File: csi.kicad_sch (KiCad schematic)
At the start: 65 parts, among them J1 Conn_01x15_MountingPin, J16 Conn_01x15_MountingPin, J6 Conn_01x15_MountingPin, J9 Conn_01x15_MountingPin, U24 AP22615A_TSOT26, U25 AP22615A_TSOT26, U26 PI4MSD5V9548AZDEX, U3 AP22615A_TSOT26, U31 NTS0102_XSON, U32 NTS0102_XSON, U7 AP22615A_TSOT26

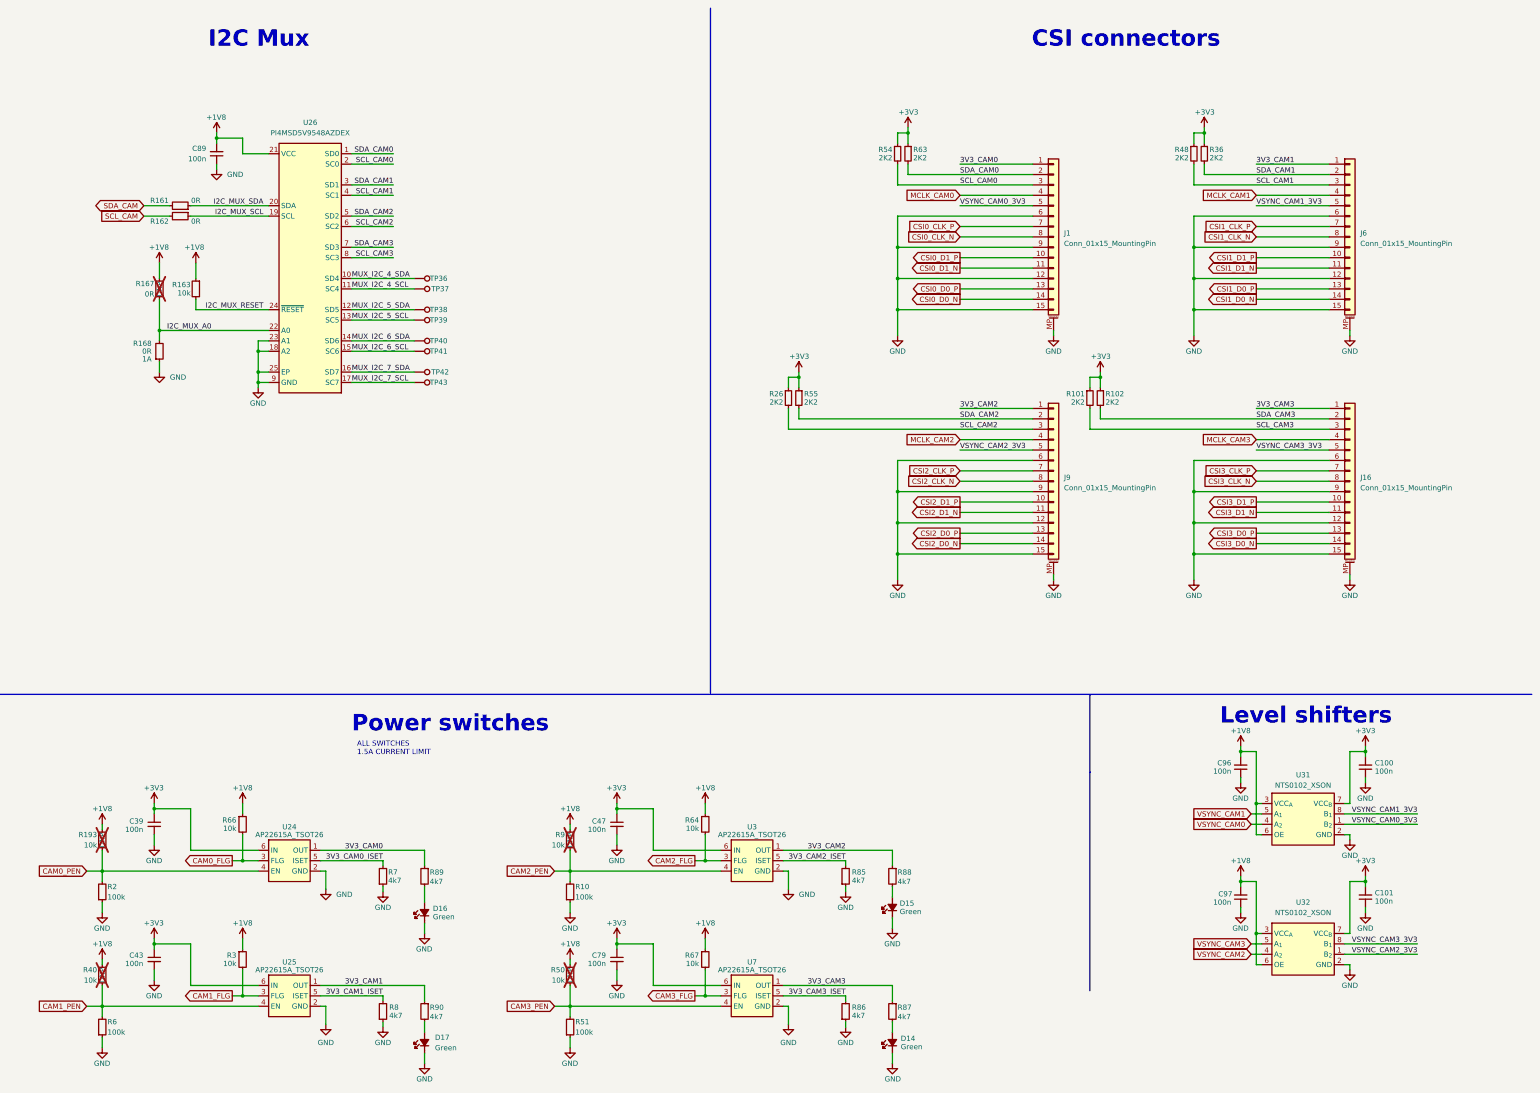
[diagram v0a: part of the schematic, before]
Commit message: Schematic Cleanup, Complete routing
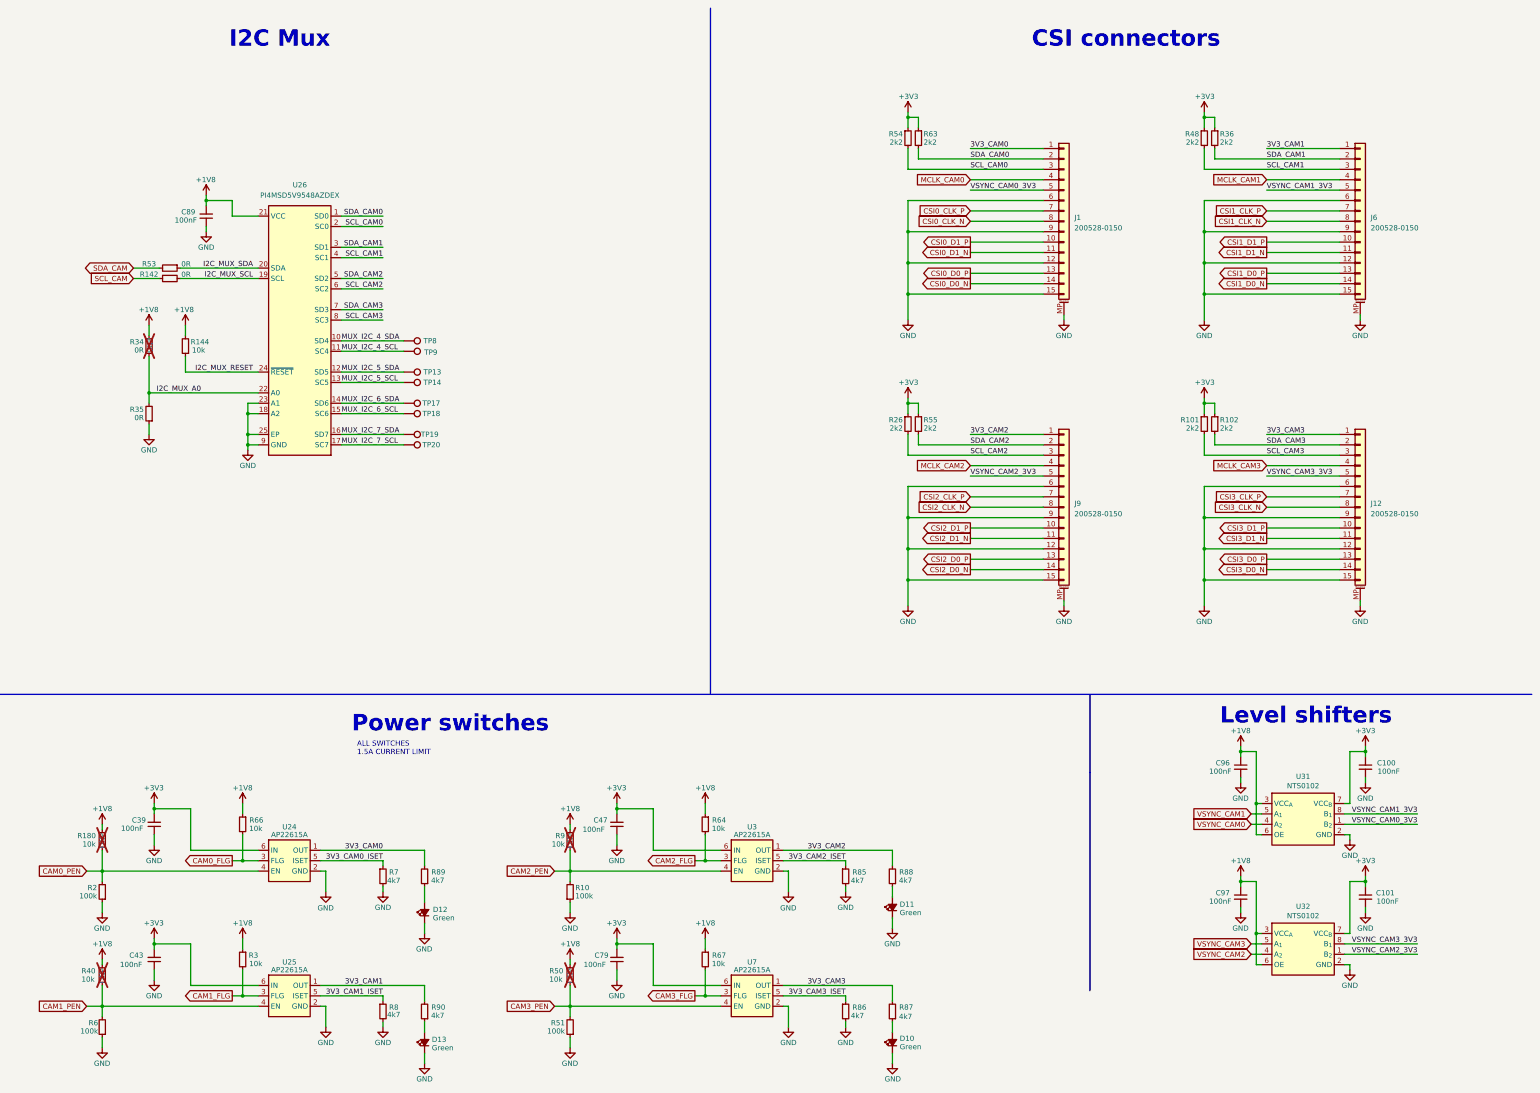
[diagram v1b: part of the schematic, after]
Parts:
- C100, C101, C39, C43, C47, C79, C89, C96, C97: value C_100n_0603 -> 100nF; symbol antmicroCapacitors0402:C_100n_0402 -> Device:C_Small
- D10: renamed from D14; symbol antmicroLEDIndicationDiscrete:LED_G_0603_LTST-C190GKT -> Device:LED_Small_Filled
- D11: renamed from D15; symbol antmicroLEDIndicationDiscrete:LED_G_0603_LTST-C190GKT -> Device:LED_Small_Filled
- D12: renamed from D16; symbol antmicroLEDIndicationDiscrete:LED_G_0603_LTST-C190GKT -> Device:LED_Small_Filled
- D13: renamed from D17; symbol antmicroLEDIndicationDiscrete:LED_G_0603_LTST-C190GKT -> Device:LED_Small_Filled
- J1, J6, J9: value Conn_01x15_MountingPin -> 200528-0150
- J12: renamed from J16; value Conn_01x15_MountingPin -> 200528-0150
- R10, R2, R51, R6: value R_100k_0603 -> 100k; symbol antmicroResistors0402:R_100k_0402 -> Device:R_Small
- R101, R102, R26, R36, R48, R54, R55, R63: value 2K2 -> 2k2
- R142: renamed from R162; value R_0R_0402 -> 0R; symbol antmicroResistors0402:R_0R_0402 -> Device:R_Small
- R144: renamed from R163; value R_10k_0603 -> 10k; symbol antmicroResistors0402:R_10k_0402 -> Device:R_Small
- R180: renamed from R193; value R_10k_0603 -> 10k; symbol antmicroResistors0402:R_10k_0402 -> Device:R_Small; now in the parts list
- R3, R64, R66, R67: value R_10k_0603 -> 10k; symbol antmicroResistors0402:R_10k_0402 -> Device:R_Small
- R34: renamed from R167; value R_0R_0402 -> 0R; symbol antmicroResistors0402:R_0R_0402 -> Device:R_Small; now in the parts list
- R35: renamed from R168; value R_0R_0402 -> 0R; symbol antmicroResistors0402:R_0R_0402 -> Device:R_Small
- R40, R50, R9: value R_10k_0603 -> 10k; symbol antmicroResistors0402:R_10k_0402 -> Device:R_Small; now in the parts list
- R53: renamed from R161; value R_0R_0402 -> 0R; symbol antmicroResistors0402:R_0R_0402 -> Device:R_Small
- R7, R8, R85, R86, R87, R88, R89, R90: value R_4k7_0603 -> 4k7; symbol antmicroResistors0402:R_4k7_0402 -> Device:R_Small
- TP13: renamed from TP38; symbol antmicroTestPoints:TP_0.75mm_SMD -> Connector:TestPoint
- TP14: renamed from TP39; symbol antmicroTestPoints:TP_0.75mm_SMD -> Connector:TestPoint
- TP17: renamed from TP40; symbol antmicroTestPoints:TP_0.75mm_SMD -> Connector:TestPoint
- TP18: renamed from TP41; symbol antmicroTestPoints:TP_0.75mm_SMD -> Connector:TestPoint
- TP19: renamed from TP42; symbol antmicroTestPoints:TP_0.75mm_SMD -> Connector:TestPoint
- TP20: renamed from TP43; symbol antmicroTestPoints:TP_0.75mm_SMD -> Connector:TestPoint
- TP8: renamed from TP36; symbol antmicroTestPoints:TP_0.75mm_SMD -> Connector:TestPoint
- TP9: renamed from TP37; symbol antmicroTestPoints:TP_0.75mm_SMD -> Connector:TestPoint
- U24, U25, U3, U7: value AP22615A_TSOT26 -> AP22615A; symbol antmicroPMICPowerDistributionSwitchesLoadDrivers:AP22615A_TSOT26 -> JetsonCarrier:AP22615A_TSOT26
- U26: symbol antmicroLogicSignalSwitchesMultiplexersDecoders:PI4MSD5V9548AZDEX -> JetsonCarrier:PI4MSD5V9548AZDEX
- U31, U32: value NTS0102_XSON -> NTS0102; symbol antmicroLogicTranslatorsLevelShifters:NTS0102_XSON -> JetsonCarrier:NTS0102
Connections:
- net +1V8: now also C96.1, C97.1, R144.2, R180.1, R40.1, R50.1, R9.1; no longer C96.2, C97.2, R144.1, R180.2, R40.2, R50.2, R9.2
- net +3V3: now also C100.1, C101.1, C39.2, C43.2, C47.2, C79.2; no longer C100.2, C101.2, C39.1, C43.1, C47.1, C79.1
- net 3V3_CAM0: now also R89.2; no longer R89.1
- net 3V3_CAM0_ISET: now also R7.1; no longer R7.2
- net 3V3_CAM1: now also R90.2; no longer R90.1
- net 3V3_CAM1_ISET: now also R8.1; no longer R8.2
- net 3V3_CAM2: now also R88.2; no longer R88.1
- net 3V3_CAM2_ISET: now also R85.1; no longer R85.2
- net 3V3_CAM3: now also R87.2; no longer R87.1
- net 3V3_CAM3_ISET: now also R86.1; no longer R86.2
- net CAM0_PEN: now also R180.2; no longer R180.1
- net CAM1_PEN: now also R40.2; no longer R40.1
- net CAM2_PEN: now also R9.2; no longer R9.1
- net CAM3_PEN: now also R50.2; no longer R50.1
- net GND: now also C100.2, C101.2, C39.1, C43.1, C47.1, C79.1, C96.2, C97.2, R7.2, R8.2, R85.2, R86.2; no longer C100.1, C101.1, C39.2, C43.2, C47.2, C79.2, C96.1, C97.1, R7.1, R8.1, R85.1, R86.1
- net I2C_MUX_RESET: now also R144.1; no longer R144.2
- net I2C_MUX_SCL: now also R142.2; no longer R142.1
- net SCL_CAM: now also R142.1; no longer R142.2
- net at D11.2 (A): now also R88.1; no longer R88.2
- net at D10.2 (A): now also R87.1; no longer R87.2
- net at D13.2 (A): now also R90.1; no longer R90.2
- net at D12.2 (A): now also R89.1; no longer R89.2
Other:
- moved on the sheet: C100, C101, C39, C43, C47, C79, C89, C96, C97, J1, J12, J6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
